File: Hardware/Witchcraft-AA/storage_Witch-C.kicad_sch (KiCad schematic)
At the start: 1 part, among them J6 10157930

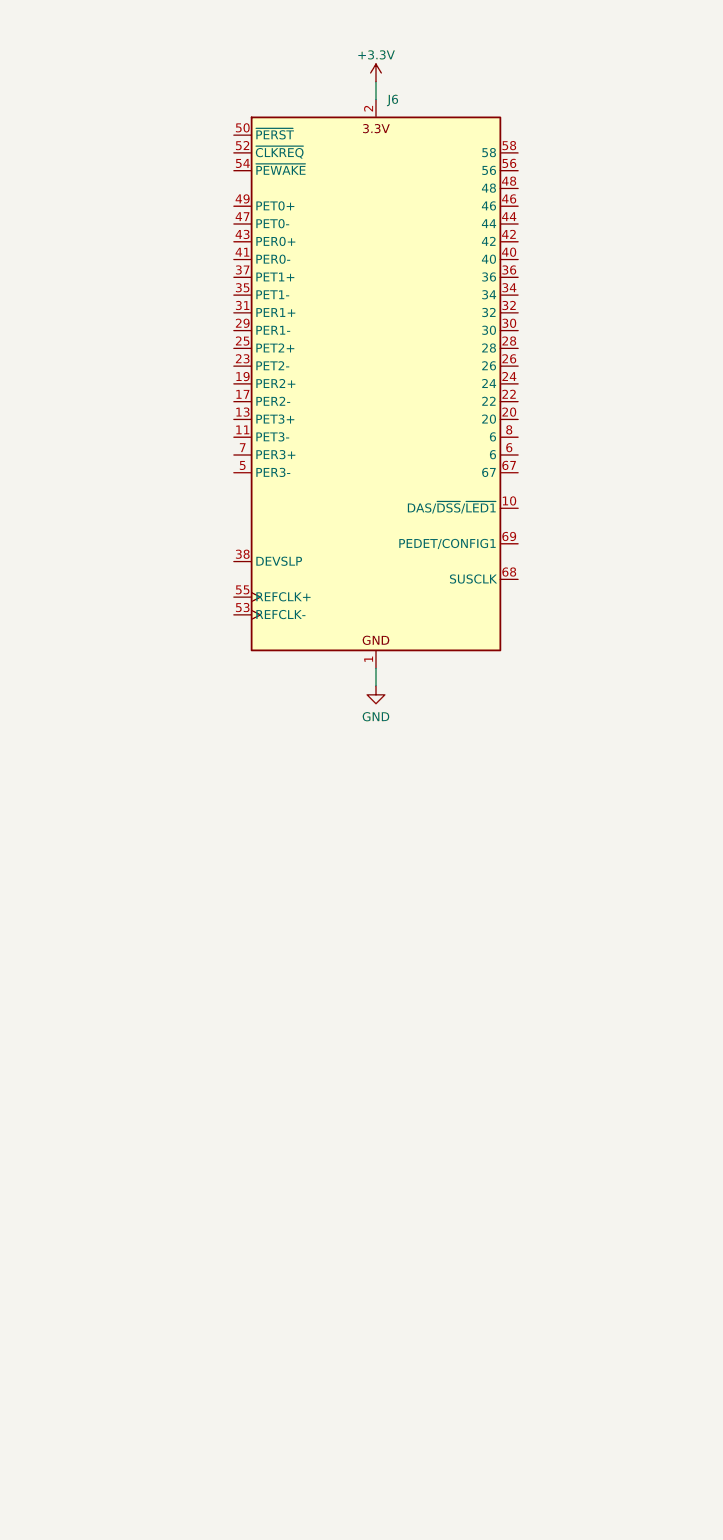
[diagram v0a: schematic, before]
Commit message: Almost completed the design of the new finstack, and have begun work on a redesign of cold-plate and rearrangement of components
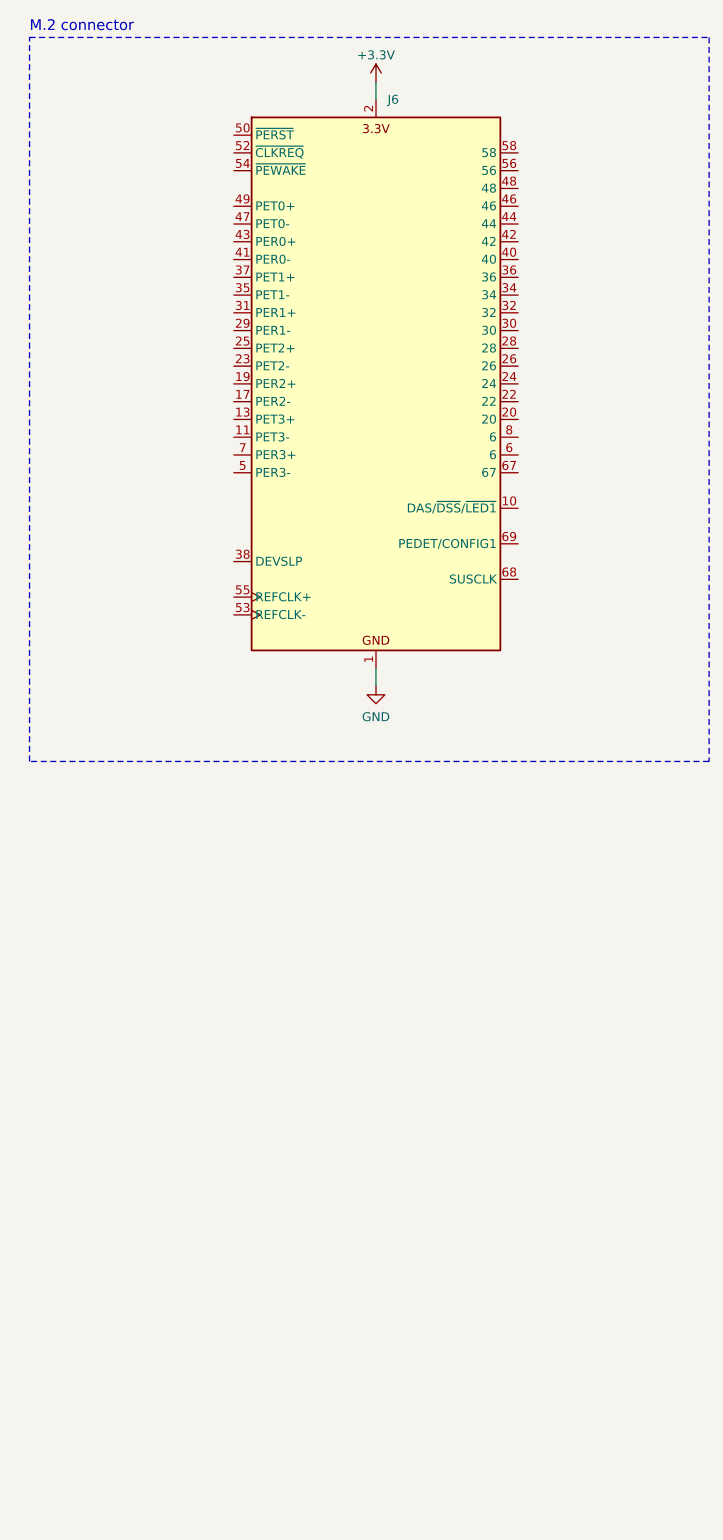
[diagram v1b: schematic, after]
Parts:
- J6: footprint LRJ:Amphenol_10157930_PCI_Express_M.2_2280_less-court -> LRJ:Amphenol_10157930_PCI_Express_M.2_2230_less-court
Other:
- note added: "M.2 connector"
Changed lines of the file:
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@@
     (stroke (width 0) (type default))
+  )
+  (rectangle (start 241.3 26.67) (end 338.455 130.175)
+    (stroke (width 0) (type dash))
+    (fill (type none))
+  )
+  (text "M.2 connector" (at 241.3 26.035 0)
+    (effects (font (size 1.524 1.524)) (justify left bottom))
   )
   (symbol (lib_id "LRJ-parts:Amphenol_10157930") (at 290.83 76.2 0) (unit 1)
@@
       (effects (font (size 1.27 1.27)) hide)
     )
-    (property "Footprint" "LRJ:Amphenol_10157930_PCI_Express_M.2_2280_less-court" (at 290.83 57.15 0)
+    (property "Footprint" "LRJ:Amphenol_10157930_PCI_Express_M.2_2230_less-court" (at 290.83 57.15 0)
       (effects (font (size 1.27 1.27)) hide)
     )

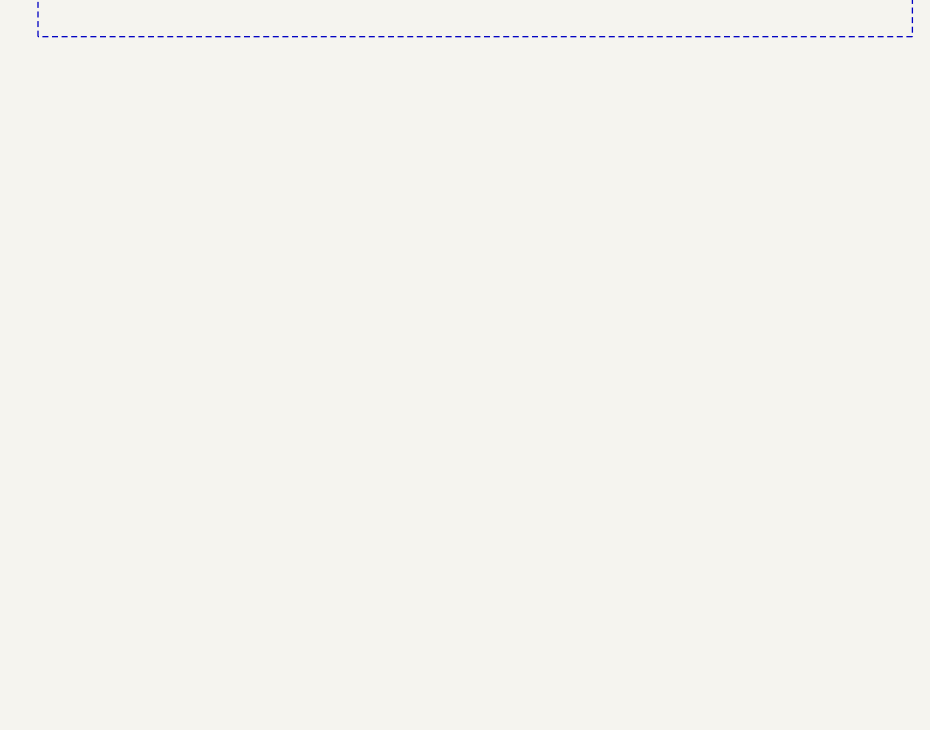
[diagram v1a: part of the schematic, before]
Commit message: Upgraded the shell-assembly to the Assembly4 workbench, allowing for better performance.
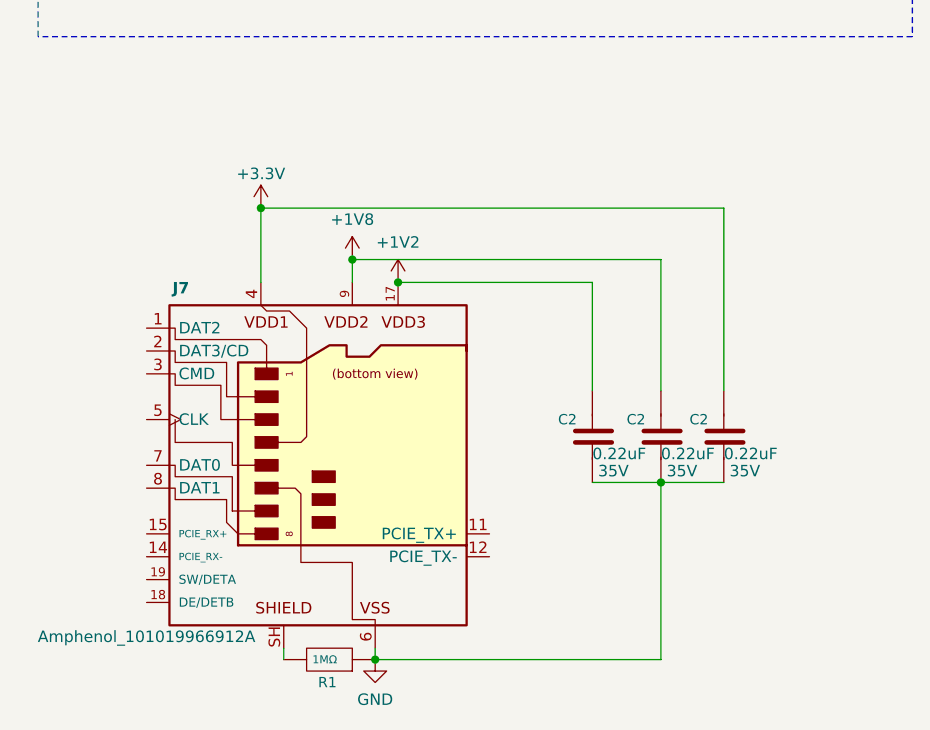
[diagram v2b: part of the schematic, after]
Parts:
- added C2 (x3): C_CGA2B1X7R1V224K, Capacitor_SMD:C_0402_1005Metric, symbol LRJ-parts:C_CGA2B1X7R1V224K
- added J7: Amphenol_101019966912A, LRJ:microSD_HC_Amphenol_101019966912A, symbol LRJ-parts:Amphenol_101019966912A
- added R1: R_ERJ-3GEYJ105V, Resistor_SMD:R_0603_1608Metric, symbol LRJ-parts:R_ERJ-3GEYJ105V
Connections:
- net +3.3V: now also C2.1, J7.4 (VDD1/3.3V)
- net GND: now also C2.2, C2.2, C2.2, J7.10 (VSS), J7.13 (VSS), J7.16 (VSS), J7.6 (VSS), R1.1
- new net: J7.SH (SHIELD), R1.2
- new net +1V2: C2.1, J7.17 (VDD3/1.2V)
- new net +1V8: C2.1, J7.9 (VDD2/1.8V)

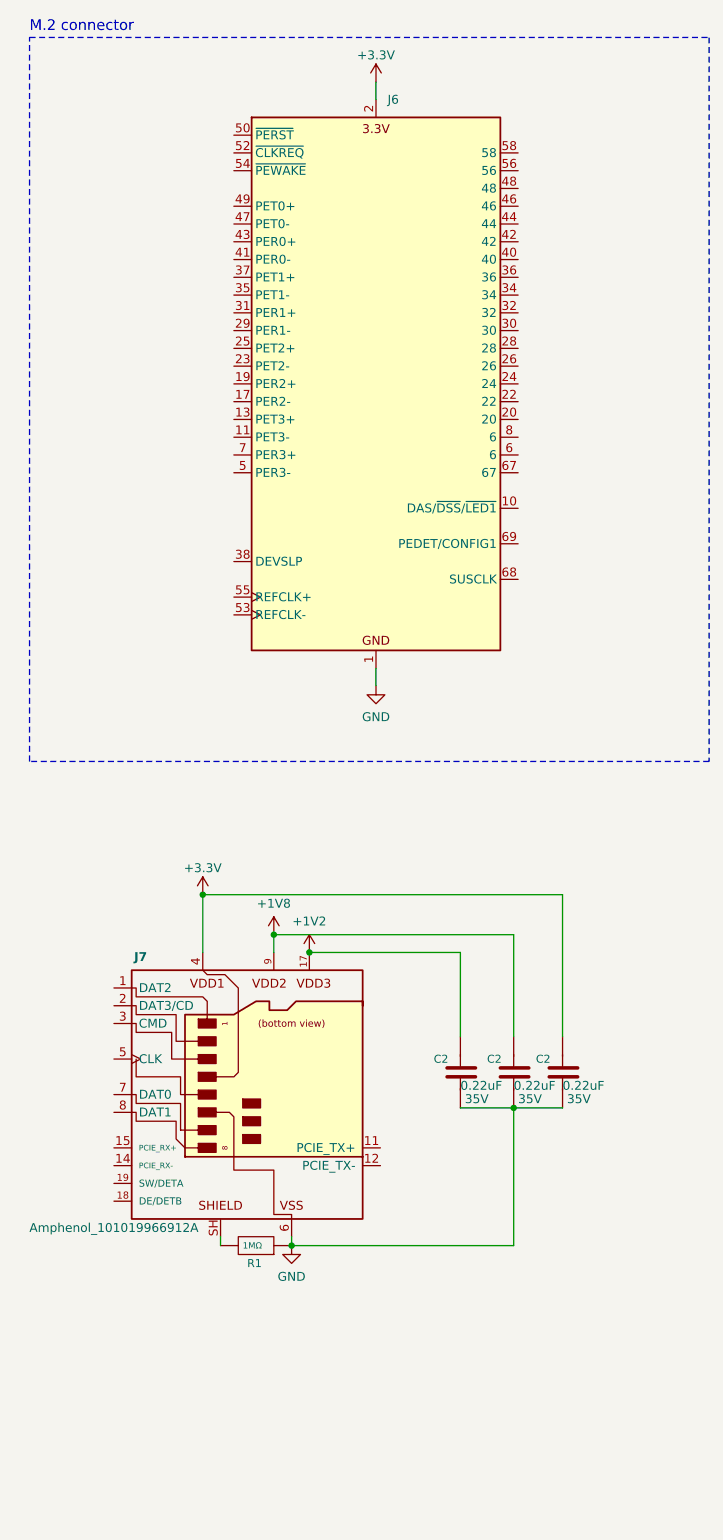
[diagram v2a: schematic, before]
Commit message: MCAD: Added Oculink connector. ECAD: Added Oculink connector.
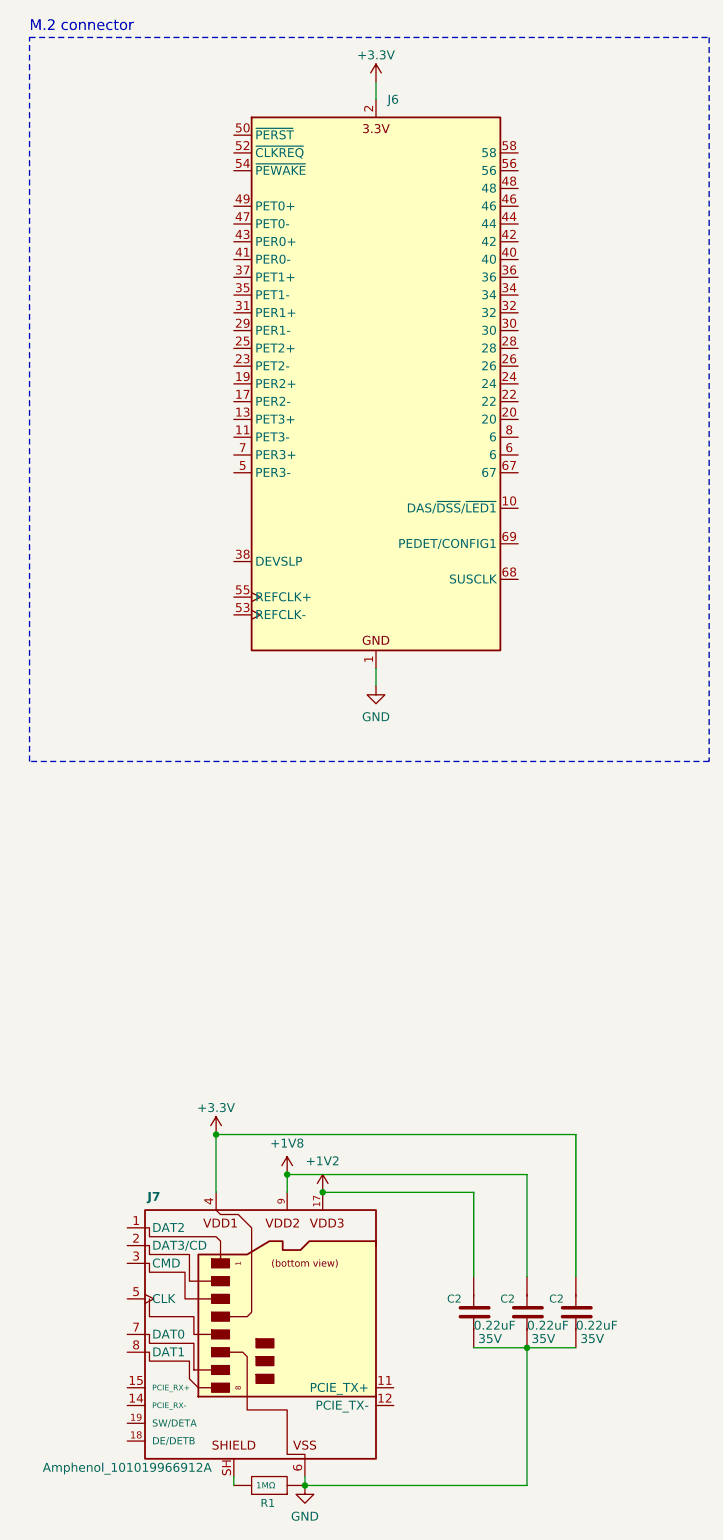
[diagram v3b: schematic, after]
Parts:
- J6: footprint LRJ:Amphenol_10157930_PCI_Express_M.2_2230_less-court -> LRJ:Amphenol_10157930_PCI_Express_M.2_2280_less-court
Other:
- title: (none) -> WITCHCRAFT HANDHELD
- moved on the sheet: C2, J7, R1
